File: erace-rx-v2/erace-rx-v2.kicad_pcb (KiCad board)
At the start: 4 copper layers, 28 x 28 mm, 59 parts, among them J1 Conn_01x08_MountingPin, J2 USB_C_Receptacle_USB2.0_16P, Q1 2N7002, Q2 2N7002, U1 ESP32-C3, U2 AMS1117-3.3, Y1 40MHz, Y2 52MHz

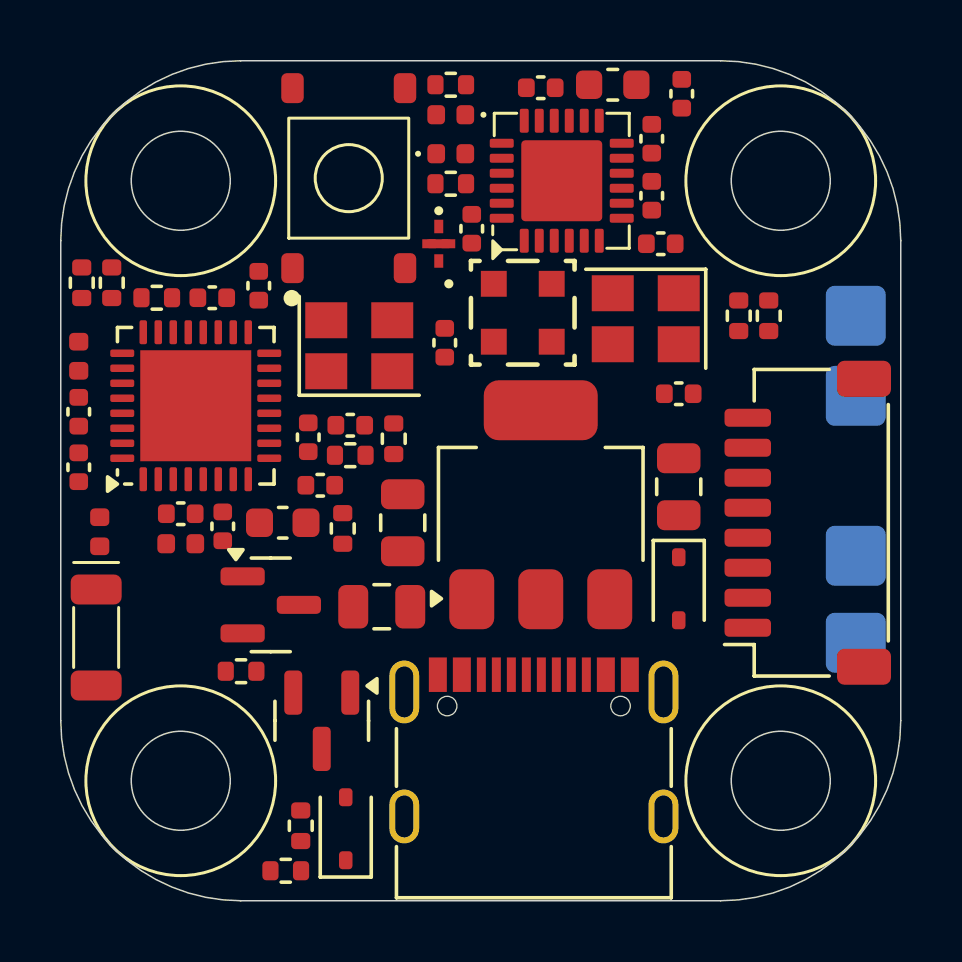
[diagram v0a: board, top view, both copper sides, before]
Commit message: 0 DRC violations :tada:
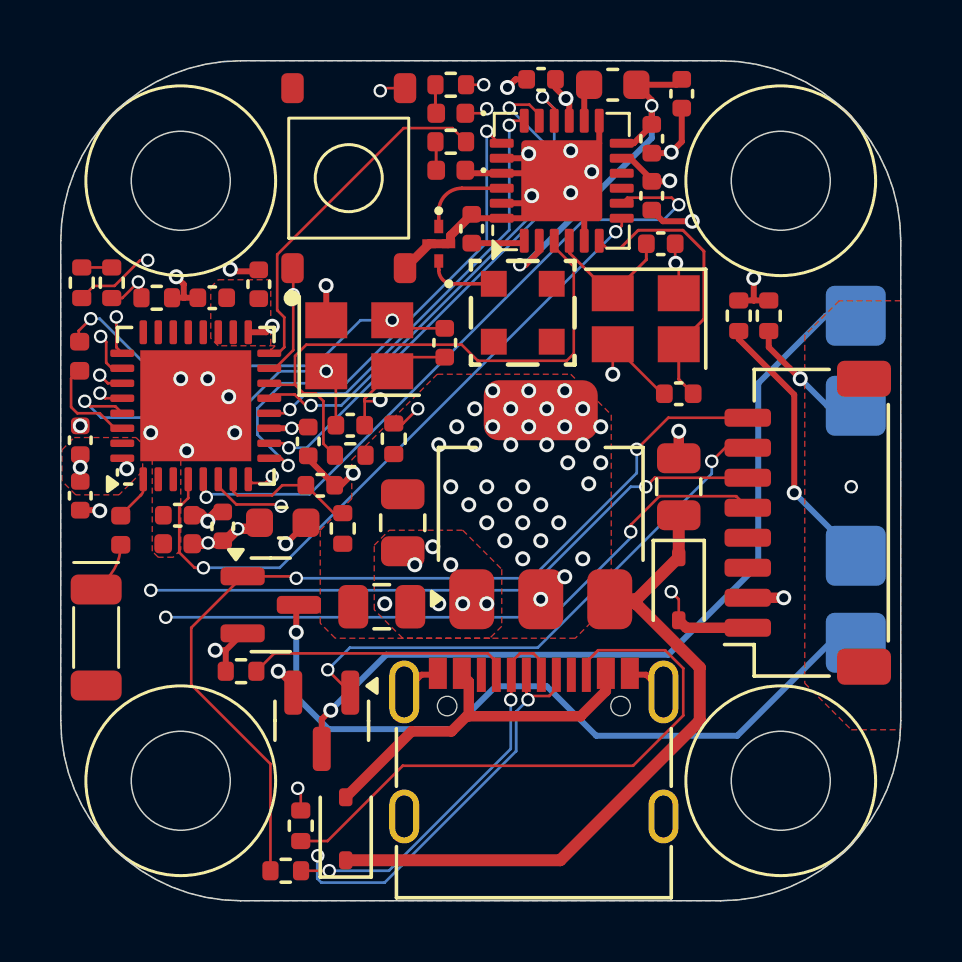
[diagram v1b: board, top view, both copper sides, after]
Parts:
- moved R11 1.40 mm to (62.0, 51.7), turned to 180 degrees
- moved C6 0.95 mm to (49.6, 63.5)
- moved C5 0.95 mm to (49.6, 61.6)
- moved L2 0.70 mm to (51.0, 64.7)
- moved D1 0.55 mm to (62.0, 52.6), turned to 180 degrees
- moved P3 0.33 mm to (75.5, 60.5)
- moved C13 0.28 mm to (65.0, 49.6)
- moved C2 0.14 mm to (57.2, 61.7)
- moved C10 0.11 mm to (52.9, 64.2)
- moved L1 0.10 mm to (52.9, 65.1)
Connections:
- net /IO18 renamed /USBD-
- net /IO19 renamed /USBD+
- BN1 pad 2: /IO9 -> unconnected-(BN1-Pad2)
- J1 pad MP: unconnected-(J1-MountPin-PadMP) -> GND
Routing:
- net GND: track 0.00 -> 52.8 mm, vias 0 -> 40
- net /USBD+: track 0.00 -> 36.2 mm, vias 0 -> 3
- net /USBD-: track 0.00 -> 36.0 mm, vias 0 -> 3
- net /IO20: track 0.00 -> 31.3 mm, vias 0 -> 3
- net /CH_4: track 0.00 -> 31.2 mm, vias 0 -> 2
- net /IO21: track 0.00 -> 29.5 mm, vias 0 -> 3
- net VCC: track 0.00 -> 28.2 mm, vias 0 -> 2
- net Net-(Q1-D): track 0.00 -> 27.9 mm, vias 0 -> 1
- net /IO3: track 0.00 -> 26.5 mm, vias 0 -> 3
- net Net-(Q2-D): track 0.00 -> 24.8 mm, vias 0 -> 1
- net Net-(D2-K): track 0.00 -> 22.9 mm
- net /IO1: track 0.00 -> 22.5 mm, vias 0 -> 2
- net /IO0: track 0.00 -> 22.5 mm, vias 0 -> 2
- net Net-(J2-CC2): track 0.00 -> 20.1 mm
- net /IO8: track 0.00 -> 18.8 mm
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- added copper zone on B.Cu, net +3V3
- added copper zone on F.Cu, net +3V3
- added copper zone on In2.Cu, net +3V3
- added copper zone on F.Cu, net GND
- added copper zone on In1.Cu, net GND
- added copper zone on F.Cu, net VDD3P3

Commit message: corrected XTAL, updated for JLC stock
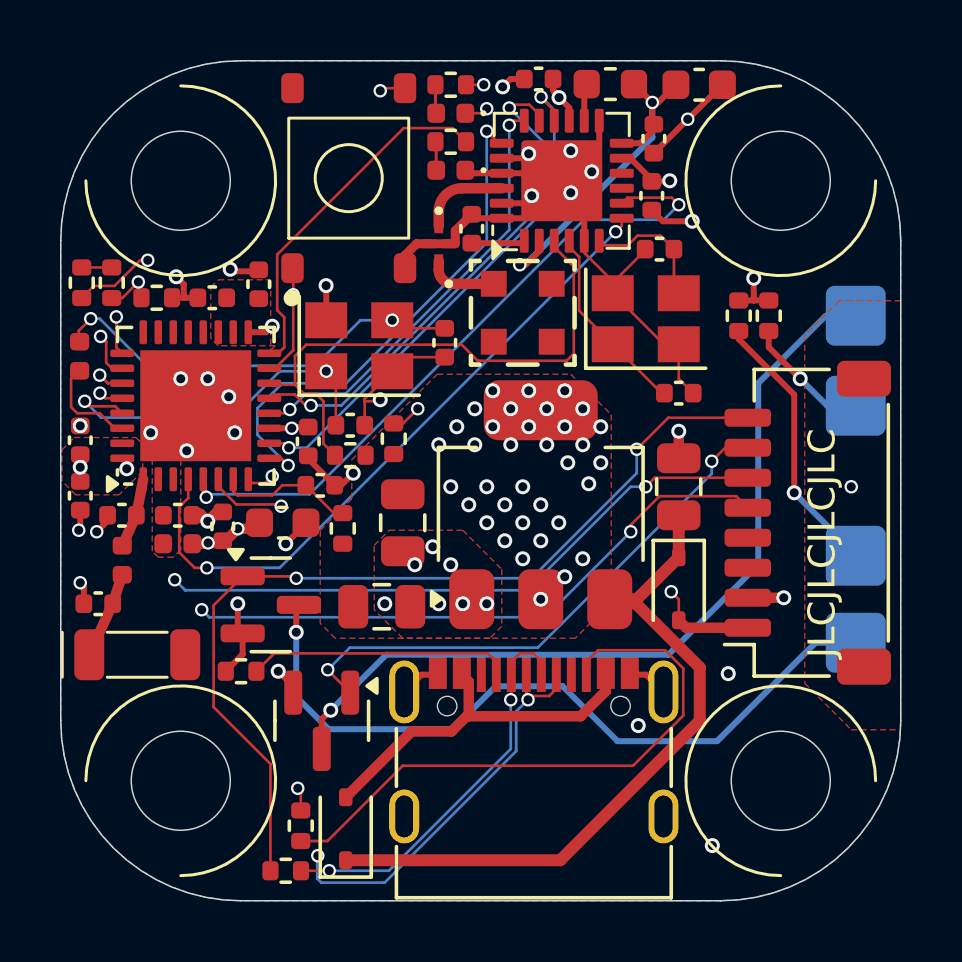
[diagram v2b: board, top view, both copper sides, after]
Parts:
- added C19: 1.2pF, Capacitor_SMD:C_0402_1005Metric, F.Cu at (51.0, 64.2)
- added C21: 1.2pF, Capacitor_SMD:C_0402_1005Metric, F.Cu at (50.2, 67.1)
- AE1: value Antenna_Shield -> ANT3216LL00R2400A
- C15: footprint Capacitor_SMD:C_0402_1005Metric -> Capacitor_SMD:C_0603_1608Metric
- L2: value 2.0nH -> 3.0nH
- moved C17 5.02 mm to (69.6, 60.1)
- moved C18 4.86 mm to (69.0, 55.3)
- moved C15 2.40 mm to (70.3, 49.8), turned to 0 degrees
- moved C16 1.76 mm to (68.8, 51.6)
- moved AE1 1.49 mm to (51.5, 68.8), turned to 0 degrees
- moved L2 1.00 mm to (51.0, 65.7)
- moved L5 0.08 mm to (67.3, 49.8)
- moved C13 0.08 mm to (64.9, 49.6)
- turned Y2 to 0 degrees
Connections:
- Y2 pad 1: GND -> Net-(RF1-XTA)
- Y2 pad 2: Net-(RF1-XTA) -> GND
- Y2 pad 3: GND -> Net-(RF1-XTB)
- Y2 pad 4: Net-(RF1-XTB) -> GND
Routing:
- net GND: track 52.8 -> 60.0 mm
- net Net-(RF1-XTB): track 9.43 -> 4.41 mm
- net Net-(RF1-XTA): track 4.52 -> 6.52 mm
- net /IO20: track 31.3 -> 30.4 mm
- net Net-(AE1-A): track 1.94 -> 2.89 mm
- net Net-(U1-LNA_IN): track 1.51 -> 2.34 mm
- net /IO21: track 29.5 -> 28.9 mm
- net /CH_4: track 31.2 -> 30.5 mm
- net +3V3: track 10.3 -> 10.6 mm, vias 45 -> 48
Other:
- board text added: "3+"
- board text added: "3-"
- board text added: "4 3 2 1 T C - +"
- board text added: "4+"
- board text added: "4-"
- board text added: "JLCJLCJLCJLC"
- board text added: "eRace-Cup ELRS RX V2"
- board text added: "github.com/bastian2001 /erace-cup-receiver"

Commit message: adjusted for Johanson filter, moved power LED
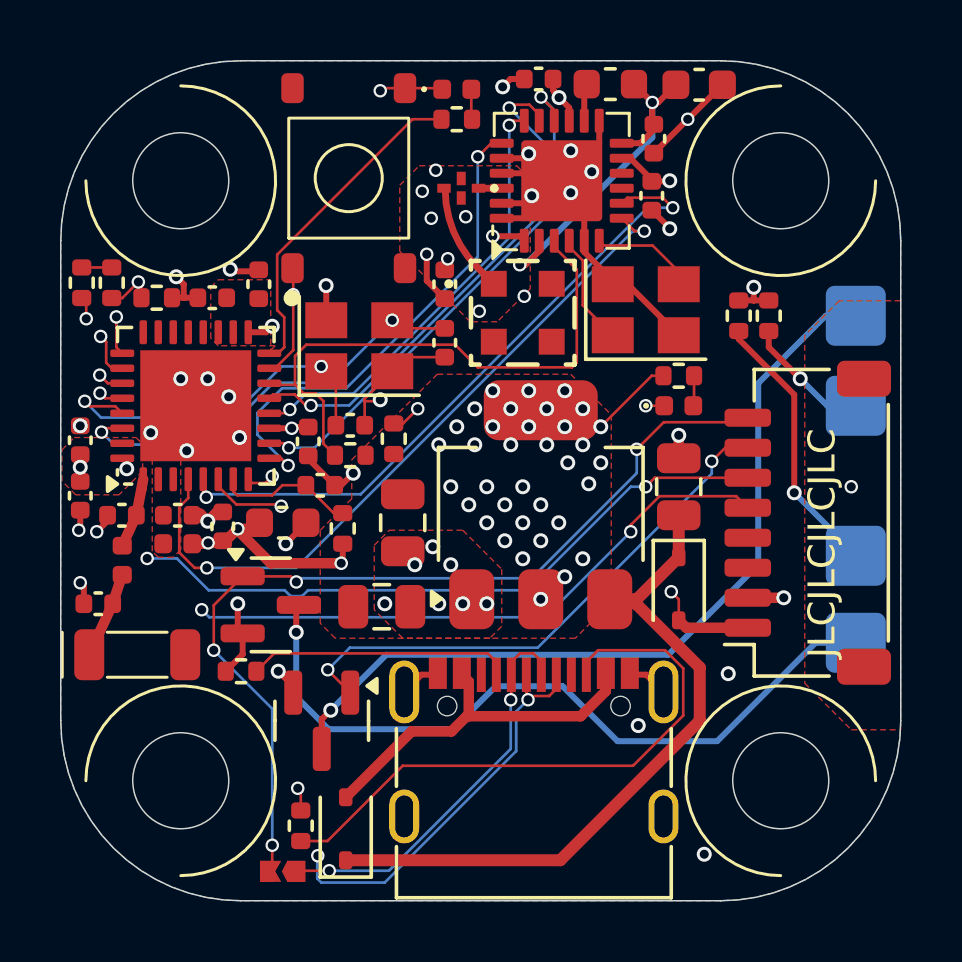
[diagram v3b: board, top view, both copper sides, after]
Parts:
- removed C17, C18: TBD, Capacitor_SMD:C_0402_1005Metric
- removed L4: TBD, Inductor_SMD:L_0402_1005Metric
- removed R13: 0R, Resistor_SMD:R_0402_1005Metric
- added JP1: Jumper_2_Small_Open, components:solder bridge, F.Cu at (56.4, 76.0)
- AE2: value 0479480001 -> 479480001
- moved D3 12.4 mm to (69.6, 60.5), turned to 0 degrees
- moved R4 12.3 mm to (69.6, 59.5), turned to 0 degrees
- moved D1 2.71 mm to (62.2, 50.0), turned to 0 degrees
- moved C14 2.06 mm to (61.8, 56.5)
- moved FL1 2.00 mm to (62.4, 53.2), turned to 180 degrees
- moved R11 0.78 mm to (62.2, 51.0), turned to 0 degrees
- moved Y2 0.30 mm to (68.5, 57.3)
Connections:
- C7 pad 1: Net-(C7-Pad1) -> Net-(U1-XTAL_P)
- Y1 pad 3: Net-(C7-Pad1) -> Net-(U1-XTAL_P)
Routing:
- net Net-(C7-Pad1): track 14.1 -> 0.00 mm, vias 2 -> 0
- net Net-(U1-XTAL_P): track 3.31 -> 14.2 mm, vias 0 -> 2
- net GND: track 60.0 -> 50.9 mm, vias 40 -> 47
- net +3V3: track 10.6 -> 17.2 mm
- net Net-(RF1-VR_PA): track 1.78 -> 5.37 mm, vias 0 -> 2
- net Net-(RF1-XTA): track 6.52 -> 3.75 mm
- net Net-(FL1-IN): track 3.01 -> 0.78 mm
- net /IO0: track 22.5 -> 23.9 mm
- net Net-(FL1-OUT): track 2.38 -> 3.70 mm
- net VCC: track 28.2 -> 29.1 mm
- net /IO10: track 12.0 -> 11.1 mm
- net Net-(RF1-XTB): track 4.41 -> 3.66 mm
- net /SS: track 17.4 -> 16.7 mm
- net /IO21: track 28.9 -> 29.4 mm
- net /CH_4: track 30.5 -> 30.7 mm, vias 2 -> 4
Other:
- outline, holes or cut-outs redrawn
- board text added: "eRace-Cup ELRS RX V2.1"
- board text removed: "eRace-Cup ELRS RX V2"

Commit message: V2.1 as ordered
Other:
- board text removed: "JLCJLCJLCJLC"
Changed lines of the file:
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@@
-		)
-	)
-	(gr_text "JLCJLCJLCJLC"
-		(at 74.9 68.91 90)
-		(layer "F.SilkS")
-		(effects
-			(font
-				(size 0.9 0.9)
-				(thickness 0.1)
-			)
-			(justify left bottom)
 		)
 	)
